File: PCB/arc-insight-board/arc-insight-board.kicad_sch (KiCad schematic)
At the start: 40 parts, among them J1 USB_C_Receptacle, J2 Conn_01x06, J3 Conn_01x05, J4 Conn_01x02, J5 Conn_01x02, J6 FPC_24PIN, J7 Conn_01x02, J8 U.FL, M1 Electret, U1 ESP32-S3, U2 MAX98357A, U3 MAX98357A, U4 TP4054, U5 Comparator, U6 ME6211C33M5, Y1 40MHz

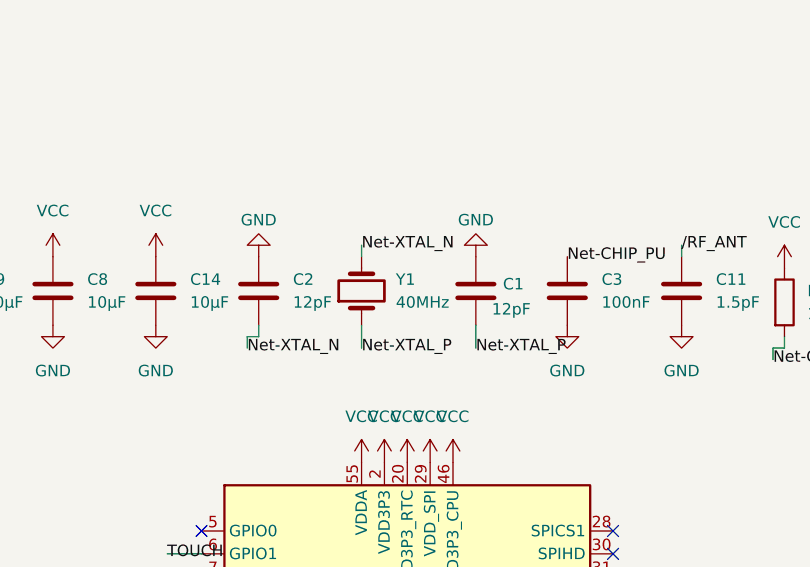
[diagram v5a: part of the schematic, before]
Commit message: Fix U1 (ESP32-S3FN8/C2913196) and Y1 (2520 4-pin crystal/C37635359); update BOMs, gerbers, positions
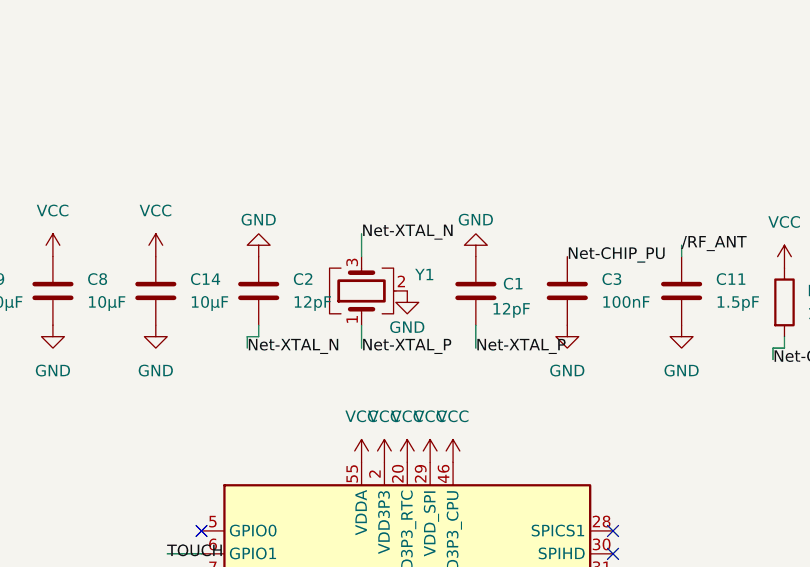
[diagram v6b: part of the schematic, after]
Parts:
- removed Y1: 40MHz, Crystal:Crystal_SMD_3215-2Pin_3.2x1.5mm, symbol Device:Crystal
- added Y1: 40MHz, Crystal:Crystal_SMD_2520-4Pin_2.5x2.0mm, symbol Device:Crystal_GND24
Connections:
- net GND: now also Y1.2 (G), Y1.4 (G)
- net Net-XTAL_N: now also Y1.3
- net Net-XTAL_P: now also Y1.1
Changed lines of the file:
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@@
 	(wire
 		(pts
+			(xy 139.7 31.75) (xy 139.7 34.29)
+		)
+		(stroke
+			(width 0)
+			(type default)
+		)
+	)
+	(wire
+		(pts
 			(xy 43.18 53.34) (xy 40.64 53.34)
 		)
@@
 	(wire
 		(pts
-			(xy 139.7 44.45) (xy 139.7 41.91)
-		)
-		(stroke
-			(width 0)
-			(type default)
-		)
-	)
-	(wire
-		(pts
 			(xy 96.52 139.7) (xy 96.52 142.24)
 		)
@@
 	(wire
 		(pts
-			(xy 77.47 48.26) (xy 78.74 48.26)
+			(xy 139.7 41.91) (xy 139.7 44.45)
 		)
 		(stroke
@@
 	(wire
 		(pts
-			(xy 139.7 33.02) (xy 139.7 34.29)
+			(xy 77.47 48.26) (xy 78.74 48.26)
 		)
 		(stroke
@@
 	)
 	(label "Net-XTAL_N"
-		(at 139.7 33.02 0)
+		(at 139.7 31.75 0)
 		(effects
 			(font
@@
 	)
 	(symbol
-		(lib_id "Device:Crystal")
-		(at 139.7 38.1 90)
-		(unit 1)
-		(body_style 1)
-		(exclude_from_sim no)
-		(in_bom yes)
-		(on_board yes)
-		(in_pos_files yes)
-		(dnp no)
-		(fields_autoplaced yes)
-		(property "Reference" "Y1"
-			(at 143.51 36.8299 90)
-			(show_name no)
-			(do_not_autoplace no)
-			(effects
-				(font
-					(size 1.27 1.27)
-				)
-				(justify right)
-			)
-		)
-		(property "Value" "40MHz"
-			(at 143.51 39.3699 90)
-			(show_name no)
-			(do_not_autoplace no)
-			(effects
-				(font
-					(size 1.27 1.27)
-				)
-				(justify right)
-			)
-		)
-		(property "Footprint" "Crystal:Crystal_SMD_3215-2Pin_3.2x1.5mm"
-			(at 139.7 38.1 0)
-			(hide yes)
-			(show_name no)
-			(do_not_autoplace no)
-			(effects
-				(font
-					(size 1.27 1.27)
-				)
-			)
-		)
-		(property "Datasheet" ""
-			(at 139.7 38.1 0)
-			(hide yes)
-			(show_name no)
-			(do_not_autoplace no)
-			(effects
-				(font
-					(size 1.27 1.27)
-				)
-			)
-		)
-		(property "Description" "Two pin crystal"
-			(at 139.7 38.1 0)
-			(hide yes)
-			(show_name no)
-			(do_not_autoplace no)
-			(effects
-				(font
-					(size 1.27 1.27)
-				)
-			)
-		)
-		(property "LCSC Part #" ""
-			(at 139.7 38.1 0)
-			(hide yes)
-			(show_name no)
-			(do_not_autoplace no)
-			(effects
-				(font
-					(size 1.27 1.27)
-				)
-			)
-		)
-		(pin "2"
-		)
-		(pin "1"
-		)
-		(instances
-			(project "arc-insight-board"
-				(path "/3d5c18af-1088-4b6c-994b-ff2dcc8d5ef3"
-					(reference "Y1")
-					(unit 1)
-				)
-			)
-		)
-	)
-	(symbol
 		(lib_id "MCU_Espressif:ESP32-S3")
 		(at 144.78 95.25 0)
@@
 	)
 	(symbol
+		(lib_id "power:GND")
+		(at 144.78 38.1 0)
+		(unit 1)
+		(body_style 1)
+		(exclude_from_sim no)
+		(in_bom yes)
+		(on_board yes)
+		(in_pos_files yes)
+		(dnp no)
+		(property "Reference" "#PWR02"
+			(at 144.78 44.45 0)
+			(hide yes)
+			(show_name no)
+			(do_not_autoplace no)
+			(effects
+				(font
+					(size 1.27 1.27)
+				)
+			)
+		)
+		(property "Value" "GND"
+			(at 144.78 42.164 0)
+			(show_name no)
+			(do_not_autoplace no)
+			(effects
+				(font
+					(size 1.27 1.27)
+				)
+			)
+		)
+		(property "Footprint" ""
+			(at 144.78 38.1 0)
+			(hide yes)
+			(show_name no)
+			(do_not_autoplace no)
+			(effects
+				(font
+					(size 1.27 1.27)
+				)
+			)
+		)
+		(property "Datasheet" ""
+			(at 144.78 38.1 0)
+			(hide yes)
+			(show_name no)
+			(do_not_autoplace no)
+			(effects
+				(font
+					(size 1.27 1.27)
+				)
+			)
+		)
+		(property "Description" "Power symbol creates a global label with name \"GND\" , ground"
+			(at 144.78 38.1 0)
+			(hide yes)
+			(show_name no)
+			(do_not_autoplace no)
+			(effects
+				(font
+					(size 1.27 1.27)
+				)
+			)
+		)
+		(pin "1"
+		)
+		(instances
+			(project "arc-insight-board"
+				(path "/3d5c18af-1088-4b6c-994b-ff2dcc8d5ef3"
+					(reference "#PWR02")
+					(unit 1)
+				)
+			)
+		)
+	)
+	(symbol
 		(lib_id "Device:C")
 		(at 205.74 39.37 0)
@@
 					(unit 1)
 				)
+			)
+		)
+	)
+	(symbol
+		(lib_id "Device:Crystal_GND24")
+		(at 139.7 38.1 90)
+		(unit 1)
+		(body_style 1)
+		(exclude_from_sim no)
+		(in_bom yes)
+		(on_board yes)
+		(in_pos_files yes)
+		(dnp no)
+		(property "Reference" "Y1"
+			(at 147.828 36.322 90)
+			(show_name no)
+			(do_not_autoplace no)
+			(effects
+				(font
+					(size 1.27 1.27)
+				)
+				(justify left)
+			)
+		)
+		(property "Value" "40MHz"
+			(at 147.32 41.91 90)
+			(hide yes)
+			(show_name no)
+			(do_not_autoplace no)
+			(effects
+				(font
+					(size 1.27 1.27)
+				)
+				(justify left)
+			)
+		)
+		(property "Footprint" "Crystal:Crystal_SMD_2520-4Pin_2.5x2.0mm"
+			(at 139.7 38.1 0)
+			(hide yes)
+			(show_name no)
+			(do_not_autoplace no)
+			(effects
+				(font
+					(size 1.27 1.27)
+				)
+			)
+		)
+		(property "Datasheet" ""
+			(at 139.7 38.1 0)
+			(hide yes)
+			(show_name no)
+			(do_not_autoplace no)
+			(effects
+				(font
+					(size 1.27 1.27)
+				)
+			)
+		)
+		(property "Description" "Four pin crystal, GND on pins 2 and 4"
+			(at 139.7 38.1 0)
+			(hide yes)
+			(show_name no)
+			(do_not_autoplace no)
+			(effects
+				(font
+					(size 1.27 1.27)
+				)
+			)
+		)
+		(property private "KLC_S3.3" "The rectangle is not a symbol body but a graphical element"
+			(at 152.4 38.1 0)
+			(hide yes)
+			(show_name yes)
+			(do_not_autoplace no)
+			(effects
+				(font
+					(size 1.27 1.27)
+				)
+			)
+		)
+		(property private "KLC_S4.1" "Some pins are on 50mil grid to make the symbol small"
+			(at 154.94 38.1 0)
+			(hide yes)
+			(show_name yes)
+			(do_not_autoplace no)
+			(effects
+				(font
+					(size 1.27 1.27)
+				)
+			)
+		)
+		(property "LCSC Part #" "C37635359"
+			(at 139.7 38.1 90)
+			(hide yes)
+			(show_name no)
+			(do_not_autoplace no)
+			(effects
+				(font
+					(size 1.27 1.27)
+				)
+			)
+		)
+		(pin "4"
+		)
+		(pin "2"
+		)
+		(pin "3"
+		)
+		(pin "1"
+		)
+		(instances
+			(project "arc-insight-board"
+				(path "/3d5c18af-1088-4b6c-994b-ff2dcc8d5ef3"
+					(reference "Y1")
+					(unit 1)
+				)
